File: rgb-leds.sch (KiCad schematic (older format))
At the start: 595 parts, among them Q1 IRLB8721PBF

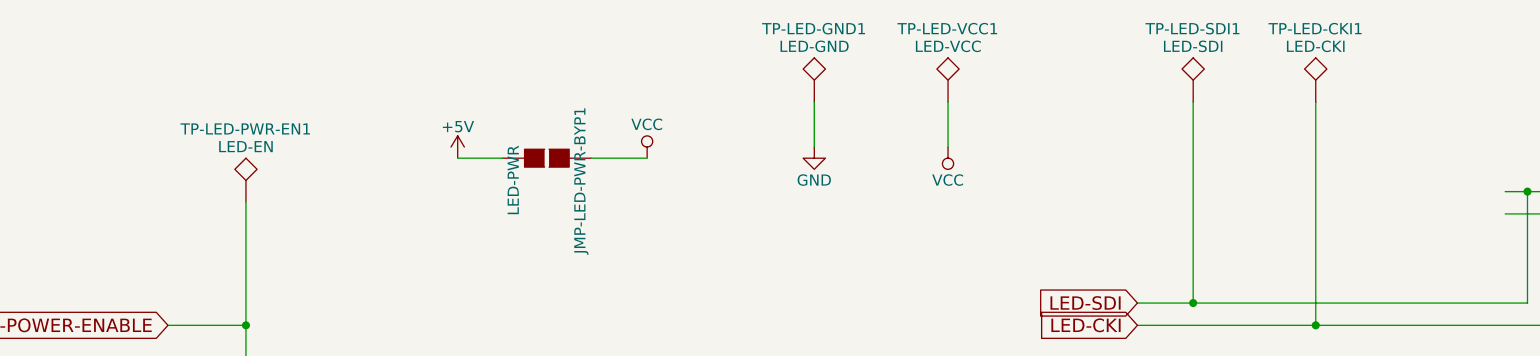
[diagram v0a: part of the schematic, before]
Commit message: tp name fixes
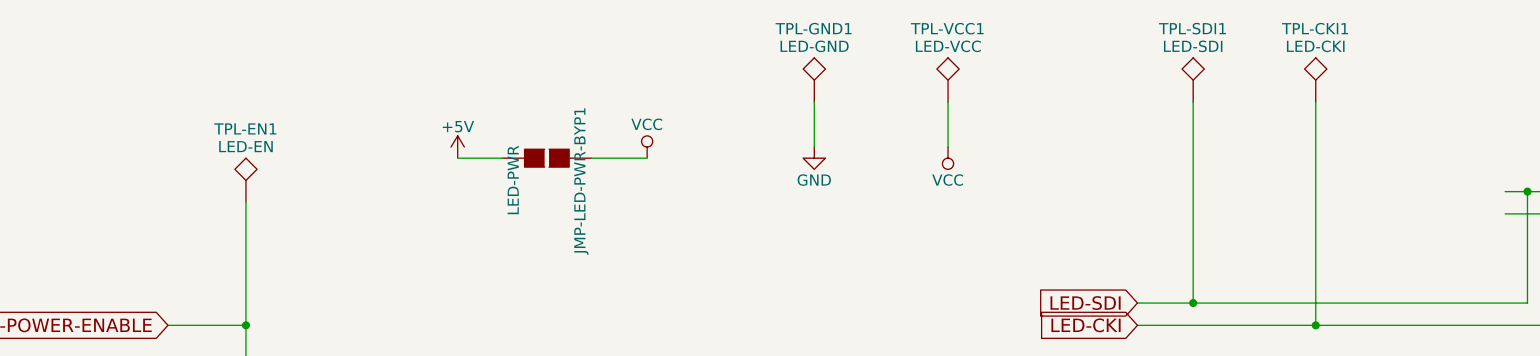
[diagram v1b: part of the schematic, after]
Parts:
- renumbered TP-LED-CKI1 to TPL-CKI1, TP-LED-PWR-EN1 to TPL-EN1, TP-LED-GND1 to TPL-GND1, TP-LED-SDI1 to TPL-SDI1, TP-LED-VCC1 to TPL-VCC1
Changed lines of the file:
@@
 LED-CKI
 $Comp
-L TEST TP-LED-CKI1
+L TEST TPL-CKI1
 U 1 1 5B3D80BC
 P -2800 -1550
-F 0 "TP-LED-CKI1" H -2800 -1250 50  0000 C BNN
+F 0 "TPL-CKI1" H -2800 -1250 50  0000 C BNN
 F 1 "LED-CKI" H -2800 -1300 50  0000 C CNN
 F 2 "Measurement_Points:Measurement_Point_Round-SMD-Pad_Small" H -2800 -1550 50  0001 C CNN
@@
 $EndComp
 $Comp
-L TEST TP-LED-SDI1
+L TEST TPL-SDI1
 U 1 1 5B3D9188
 P -3350 -1550
-F 0 "TP-LED-SDI1" H -3350 -1250 50  0000 C BNN
+F 0 "TPL-SDI1" H -3350 -1250 50  0000 C BNN
 F 1 "LED-SDI" H -3350 -1300 50  0000 C CNN
 F 2 "Measurement_Points:Measurement_Point_Round-SMD-Pad_Small" H -3350 -1550 50  0001 C CNN
@@
 Connection ~ -1750 -1050
 $Comp
-L TEST TP-LED-GND1
+L TEST TPL-GND1
 U 1 1 5B11C8D6
 P -5050 -1550
-F 0 "TP-LED-GND1" H -5050 -1250 50  0000 C BNN
+F 0 "TPL-GND1" H -5050 -1250 50  0000 C BNN
 F 1 "LED-GND" H -5050 -1300 50  0000 C CNN
 F 2 "Measurement_Points:Measurement_Point_Round-SMD-Pad_Small" H -5050 -1550 50  0001 C CNN
@@
 $EndComp
 $Comp
-L TEST TP-LED-VCC1
+L TEST TPL-VCC1
 U 1 1 5B11D084
 P -4450 -1550
-F 0 "TP-LED-VCC1" H -4450 -1250 50  0000 C BNN
+F 0 "TPL-VCC1" H -4450 -1250 50  0000 C BNN
 F 1 "LED-VCC" H -4450 -1300 50  0000 C CNN
 F 2 "Measurement_Points:Measurement_Point_Round-SMD-Pad_Small" H -4450 -1550 50  0001 C CNN
@@
 LED-POWER-ENABLE
 $Comp
-L TEST TP-LED-PWR-EN1
+L TEST TPL-EN1
 U 1 1 5B12C38C
 P -7600 -1100
-F 0 "TP-LED-PWR-EN1" H -7600 -800 50  0000 C BNN
+F 0 "TPL-EN1" H -7600 -800 50  0000 C BNN
 F 1 "LED-EN" H -7600 -850 50  0000 C CNN
 F 2 "Measurement_Points:Measurement_Point_Round-SMD-Pad_Small" H -7600 -1100 50  0001 C CNN

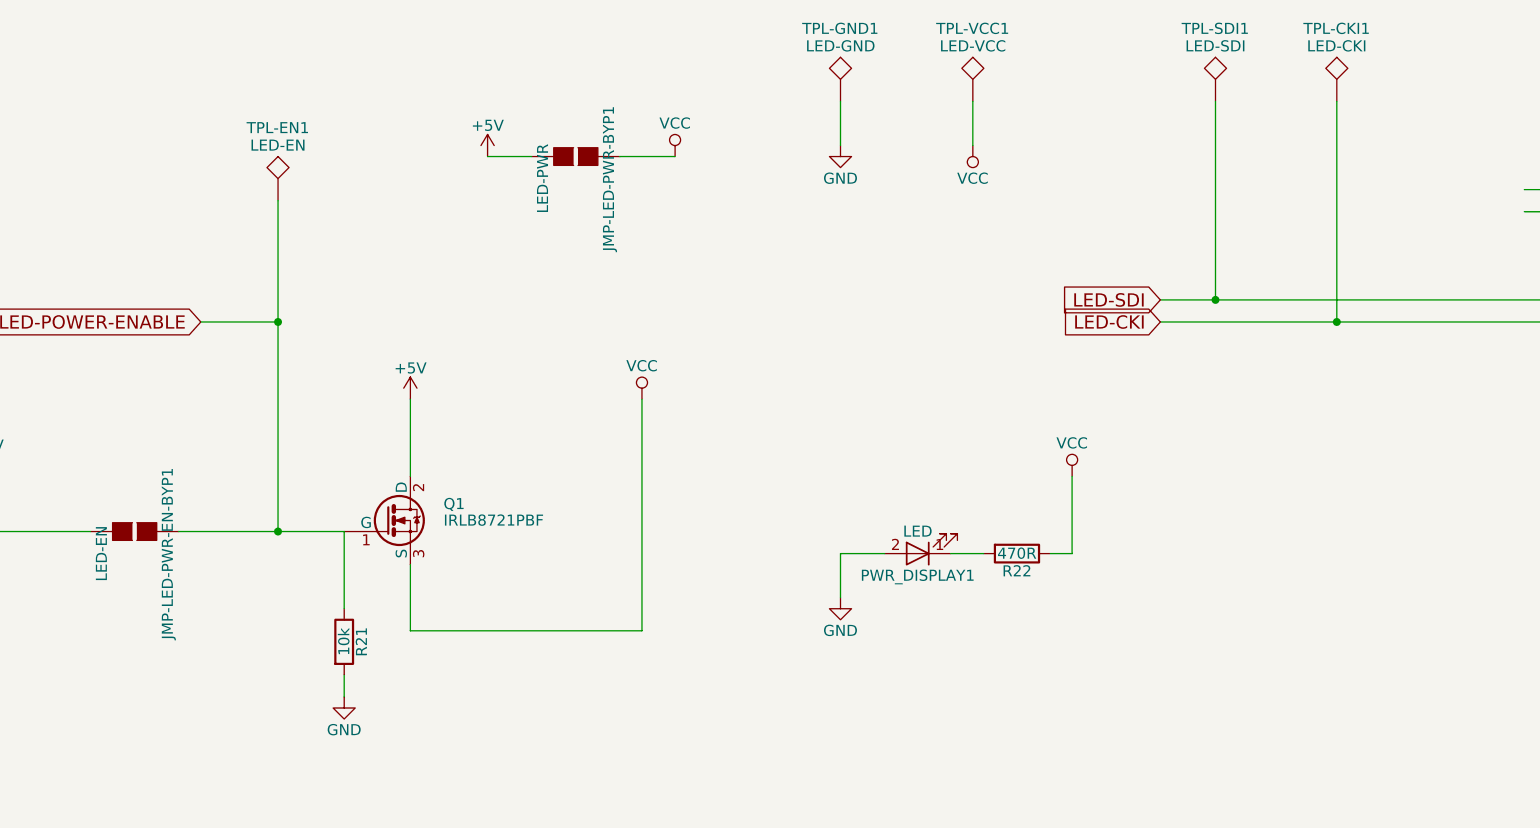
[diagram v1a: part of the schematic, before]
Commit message: Name changes on silk
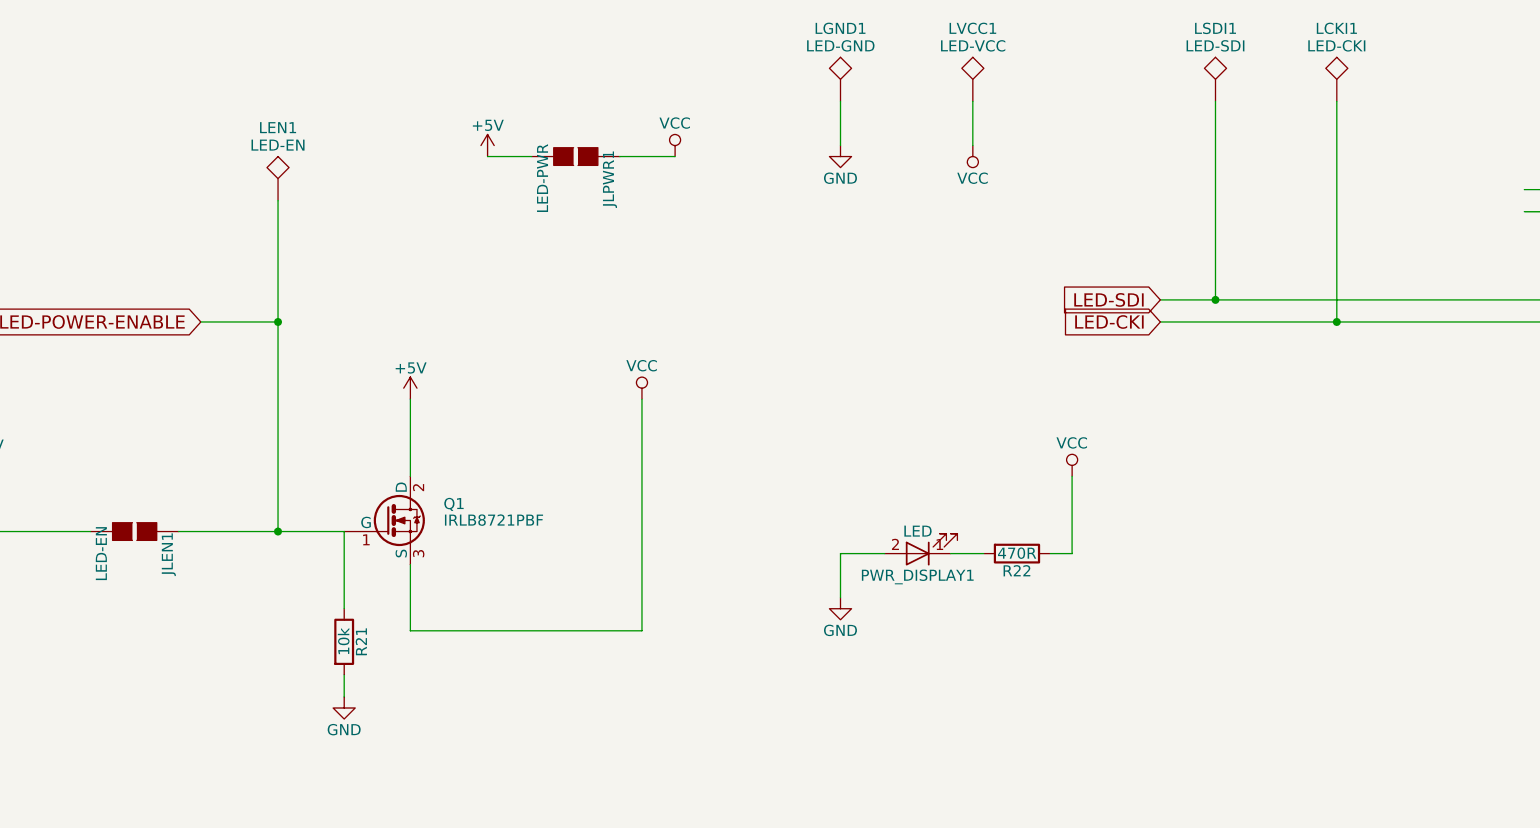
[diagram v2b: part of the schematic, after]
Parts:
- renumbered JMP-LED-PWR-EN-BYP1 to JLEN1, JMP-LED-PWR-BYP1 to JLPWR1, TPL-CKI1 to LCKI1, TPL-EN1 to LEN1, TPL-GND1 to LGND1, TPL-SDI1 to LSDI1, TPL-VCC1 to LVCC1
